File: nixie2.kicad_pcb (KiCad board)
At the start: 2 copper layers, 68.5 x 181 mm, 50 parts, among them J1 AVR-ISP-6, J14 Conn_01x10_Female, SW1 Conn_01x02_Male, SW2 Conn_01x02_Male, SW3 Conn_01x02_Male, SW4 Conn_01x02_Male, SW5 Conn_01x02_Male, SW6 Conn_01x02_Male, U1 ATmega8-16PU, U10 74141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

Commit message: Update.
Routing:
- net GND: track 461.4 -> 464.1 mm
- net Net-(C2-Pad1): track 32.9 -> 35.4 mm
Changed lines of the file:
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@@
     (thickness 1.6)
     (drawings 11)
-    (tracks 781)
+    (tracks 782)
     (zones 0)
     (modules 50)
@@
   )
   (setup
-    (last_trace_width 0.25)
+    (last_trace_width 1)
+    (user_trace_width 1)
     (trace_clearance 0.2)
     (zone_clearance 0.508)
@@
   (segment (start 89.734999 69.975001) (end 97.26 62.45) (width 0.25) (layer B.Cu) (net 4))
   (segment (start 89.545001 69.975001) (end 89.734999 69.975001) (width 0.25) (layer B.Cu) (net 4))
-  (segment (start 108.657499 50.657499) (end 106.15 53.164998) (width 0.25) (layer B.Cu) (net 4))
-  (segment (start 109.419999 49.894999) (end 108.657499 50.657499) (width 0.25) (layer B.Cu) (net 4))
-  (segment (start 86.63 68) (end 87.1 67.53) (width 0.25) (layer F.Cu) (net 4))
-  (segment (start 83 68) (end 86.63 68) (width 0.25) (layer F.Cu) (net 4))
-  (segment (start 88.175001 179.095001) (end 84.56 175.48) (width 0.25) (layer F.Cu) (net 4))
-  (segment (start 88.175001 184.864999) (end 88.175001 179.095001) (width 0.25) (layer F.Cu) (net 4))
-  (segment (start 87 186.04) (end 88.175001 184.864999) (width 0.25) (layer F.Cu) (net 4))
-  (segment (start 87 188.58) (end 87 186.04) (width 0.25) (layer F.Cu) (net 4))
-  (segment (start 87.305001 185.734999) (end 87 186.04) (width 0.25) (layer F.Cu) (net 4))
-  (segment (start 129.507082 185.734999) (end 87.305001 185.734999) (width 0.25) (layer F.Cu) (net 4))
+  (segment (start 109.419999 49.894999) (end 106.15 53.164998) (width 0.25) (layer B.Cu) (net 4))
+  (segment (start 86.63 68) (end 87.1 67.53) (width 0.25) (layer F.Cu) (net 4) (status 30))
+  (segment (start 83 68) (end 86.63 68) (width 0.25) (layer F.Cu) (net 4) (status 30))
+  (segment (start 87 188.58) (end 87 186.04) (width 0.25) (layer F.Cu) (net 4) (status 30))
+  (segment (start 87.305001 185.734999) (end 87 186.04) (width 0.25) (layer F.Cu) (net 4) (status 30))
+  (segment (start 129.507082 185.734999) (end 87.305001 185.734999) (width 0.25) (layer F.Cu) (net 4) (status 20))
   (segment (start 135 180.242081) (end 129.507082 185.734999) (width 0.25) (layer F.Cu) (net 4))
-  (segment (start 135 179.04) (end 135 180.242081) (width 0.25) (layer F.Cu) (net 4))
+  (segment (start 135 179.04) (end 135 180.242081) (width 0.25) (layer F.Cu) (net 4) (status 10))
+  (segment (start 88.202081 186.04) (end 90.5 183.742081) (width 1) (layer F.Cu) (net 4))
+  (segment (start 87 186.04) (end 88.202081 186.04) (width 1) (layer F.Cu) (net 4) (status 10))
+  (segment (start 90.5 181.42) (end 84.56 175.48) (width 1) (layer F.Cu) (net 4) (status 20))
+  (segment (start 90.5 183.742081) (end 90.5 181.42) (width 1) (layer F.Cu) (net 4))
   (segment (start 94.575001 90.245001) (end 93.45 89.12) (width 0.25) (layer B.Cu) (net 6) (status 20))
   (segment (start 107.564999 90.245001) (end 94.575001 90.245001) (width 0.25) (layer B.Cu) (net 6))
@@
   (segment (start 105.01 64.99) (end 110.355002 64.99) (width 0.25) (layer F.Cu) (net 6))
   (segment (start 104.484998 64.99) (end 105.01 64.99) (width 0.25) (layer F.Cu) (net 6))
-  (segment (start 86.53 69.5) (end 87.1 70.07) (width 0.25) (layer F.Cu) (net 6))
-  (segment (start 83 69.5) (end 86.53 69.5) (width 0.25) (layer F.Cu) (net 6))
+  (segment (start 86.53 69.5) (end 87.1 70.07) (width 0.25) (layer F.Cu) (net 6) (status 30))
+  (segment (start 83 69.5) (end 86.53 69.5) (width 0.25) (layer F.Cu) (net 6) (status 30))
   (segment (start 87.005001 79.054999) (end 97.165001 79.054999) (width 0.25) (layer F.Cu) (net 7))
   (segment (start 85.83 80.23) (end 87.005001 79.054999) (width 0.25) (layer F.Cu) (net 7) (status 10))
@@
   (segment (start 84.56 172.94) (end 94.72 172.94) (width 0.25) (layer F.Cu) (net 13) (status 30))
   (segment (start 94.72 172.94) (end 94.72 162.78) (width 0.25) (layer F.Cu) (net 13) (status 30))
-  (segment (start 83.384999 174.115001) (end 84.56 172.94) (width 0.25) (layer F.Cu) (net 13))
-  (segment (start 83.384999 179.884999) (end 83.384999 174.115001) (width 0.25) (layer F.Cu) (net 13))
-  (segment (start 87 183.5) (end 83.384999 179.884999) (width 0.25) (layer F.Cu) (net 13))
+  (segment (start 84.56 172.94) (end 81.5 176) (width 1) (layer F.Cu) (net 13) (status 10))
+  (segment (start 85.266 183.5) (end 87 183.5) (width 1) (layer F.Cu) (net 13) (status 20))
+  (segment (start 81.5 179.734) (end 85.266 183.5) (width 1) (layer F.Cu) (net 13))
+  (segment (start 81.5 176) (end 81.5 179.734) (width 1) (layer F.Cu) (net 13))
   (segment (start 87.1 64.99) (end 90.91 68.8) (width 0.25) (layer F.Cu) (net 14) (status 10))
   (segment (start 90.91 73.88) (end 94.72 77.69) (width 0.25) (layer F.Cu) (net 14) (status 20))
@@
   (segment (start 112.895002 64.115002) (end 109.96 61.18) (width 0.25) (layer B.Cu) (net 115) (status 20))
   (segment (start 113.77 64.115002) (end 112.895002 64.115002) (width 0.25) (layer B.Cu) (net 115))
-  (segment (start 134.5 168) (end 134.5 164) (width 0.25) (layer B.Cu) (net 116))
-  (segment (start 134 140) (end 134.5 140.5) (width 0.25) (layer B.Cu) (net 117))
-  (segment (start 134 135) (end 134 140) (width 0.25) (layer B.Cu) (net 117))
-  (segment (start 135.5 112.5) (end 135.5 105.5) (width 0.25) (layer B.Cu) (net 118))
-  (segment (start 135.5 84.5) (end 135.5 76.5) (width 0.25) (layer B.Cu) (net 119))
-  (segment (start 135 53) (end 135 47) (width 0.25) (layer B.Cu) (net 120))
-  (segment (start 135 30.5) (end 135 23) (width 0.25) (layer B.Cu) (net 121))
-  (segment (start 138.14999 58.68999) (end 135 55.54) (width 0.25) (layer B.Cu) (net 122))
+  (segment (start 134.5 168) (end 134.5 164) (width 0.25) (layer B.Cu) (net 116) (status 30))
+  (segment (start 134 140) (end 134.5 140.5) (width 0.25) (layer B.Cu) (net 117) (status 30))
+  (segment (start 134 135) (end 134 140) (width 0.25) (layer B.Cu) (net 117) (status 30))
+  (segment (start 135.5 112.5) (end 135.5 105.5) (width 0.25) (layer B.Cu) (net 118) (status 30))
+  (segment (start 135.5 84.5) (end 135.5 76.5) (width 0.25) (layer B.Cu) (net 119) (status 30))
+  (segment (start 135 53) (end 135 47) (width 0.25) (layer B.Cu) (net 120) (status 30))
+  (segment (start 135 30.5) (end 135 23) (width 0.25) (layer B.Cu) (net 121) (status 30))
+  (segment (start 138.14999 58.68999) (end 135 55.54) (width 0.25) (layer B.Cu) (net 122) (status 20))
   (segment (start 138.14999 84.39001) (end 138.14999 58.68999) (width 0.25) (layer B.Cu) (net 122))
-  (segment (start 135.5 87.04) (end 138.14999 84.39001) (width 0.25) (layer B.Cu) (net 122))
-  (segment (start 135 55.54) (end 137.5 53.04) (width 0.25) (layer B.Cu) (net 122))
-  (segment (start 137.5 35.54) (end 135 33.04) (width 0.25) (layer B.Cu) (net 122))
+  (segment (start 135.5 87.04) (end 138.14999 84.39001) (width 0.25) (layer B.Cu) (net 122) (status 10))
+  (segment (start 135 55.54) (end 137.5 53.04) (width 0.25) (layer B.Cu) (net 122) (status 10))
+  (segment (start 137.5 35.54) (end 135 33.04) (width 0.25) (layer B.Cu) (net 122) (status 20))
   (segment (start 137.5 53.04) (end 137.5 35.54) (width 0.25) (layer B.Cu) (net 122))
-  (segment (start 138.14999 112.39001) (end 135.5 115.04) (width 0.25) (layer B.Cu) (net 122))
+  (segment (start 138.14999 112.39001) (end 135.5 115.04) (width 0.25) (layer B.Cu) (net 122) (status 20))
   (segment (start 138.14999 89.68999) (end 138.14999 112.39001) (width 0.25) (layer B.Cu) (net 122))
-  (segment (start 135.5 87.04) (end 138.14999 89.68999) (width 0.25) (layer B.Cu) (net 122))
+  (segment (start 135.5 87.04) (end 138.14999 89.68999) (width 0.25) (layer B.Cu) (net 122) (status 10))
   (segment (start 138.14999 117.68999) (end 138.14999 123.85001) (width 0.25) (layer B.Cu) (net 122))
-  (segment (start 135.5 115.04) (end 138.14999 117.68999) (width 0.25) (layer B.Cu) (net 122))
+  (segment (start 135.5 115.04) (end 138.14999 117.68999) (width 0.25) (layer B.Cu) (net 122) (status 10))
   (segment (start 138.14999 123.85001) (end 138 124) (width 0.25) (layer B.Cu) (net 122))
-  (segment (start 138 139.54) (end 134.5 143.04) (width 0.25) (layer B.Cu) (net 122))
+  (segment (start 138 139.54) (end 134.5 143.04) (width 0.25) (layer B.Cu) (net 122) (status 20))
   (segment (start 138 124) (end 138 139.54) (width 0.25) (layer B.Cu) (net 122))
-  (segment (start 138.14999 166.89001) (end 134.5 170.54) (width 0.25) (layer B.Cu) (net 122))
+  (segment (start 138.14999 166.89001) (end 134.5 170.54) (width 0.25) (layer B.Cu) (net 122) (status 20))
   (segment (start 138.14999 146.68999) (end 138.14999 166.89001) (width 0.25) (layer B.Cu) (net 122))
-  (segment (start 134.5 143.04) (end 138.14999 146.68999) (width 0.25) (layer B.Cu) (net 122))
-  (segment (start 134.5 176) (end 135 176.5) (width 0.25) (layer B.Cu) (net 122))
-  (segment (start 134.5 170.54) (end 134.5 176) (width 0.25) (layer B.Cu) (net 122))
+  (segment (start 134.5 143.04) (end 138.14999 146.68999) (width 0.25) (layer B.Cu) (net 122) (status 10))
+  (segment (start 134.5 176) (end 135 176.5) (width 0.25) (layer B.Cu) (net 122) (status 30))
+  (segment (start 134.5 170.54) (end 134.5 176) (width 0.25) (layer B.Cu) (net 122) (status 30))
 )

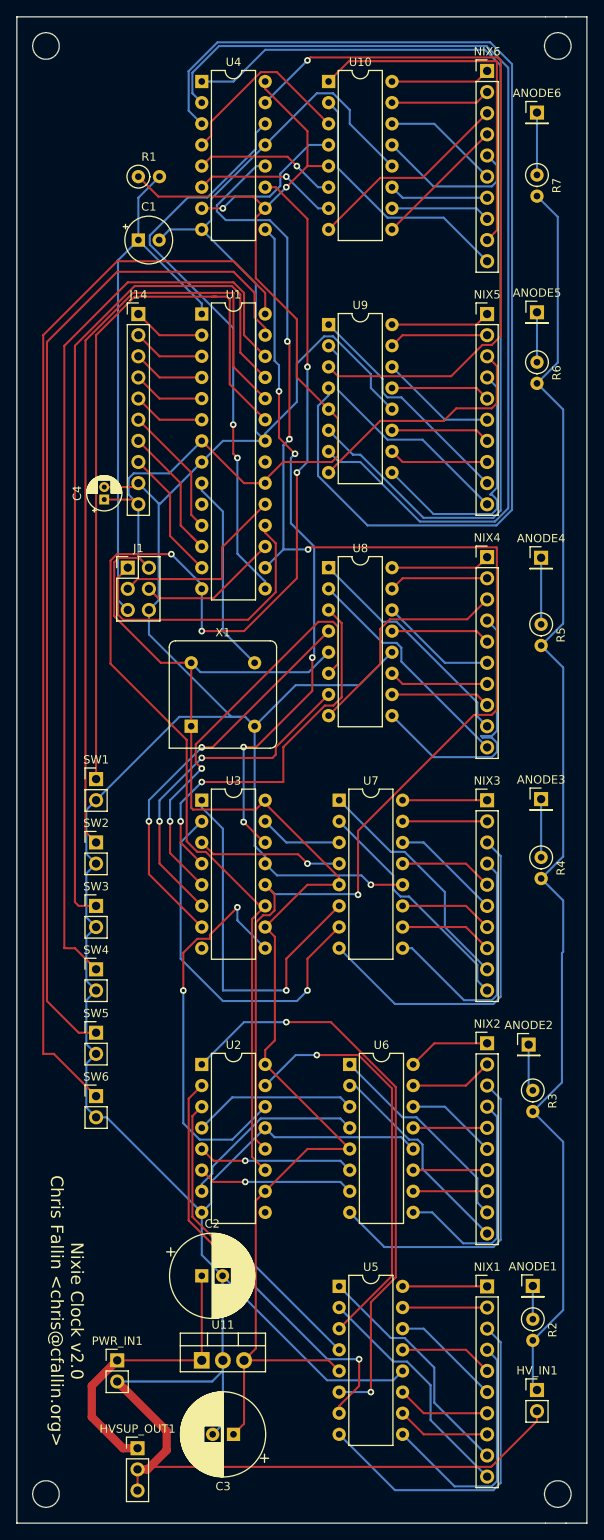
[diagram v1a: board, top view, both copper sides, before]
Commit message: Add tube adapter board, and tweak main board
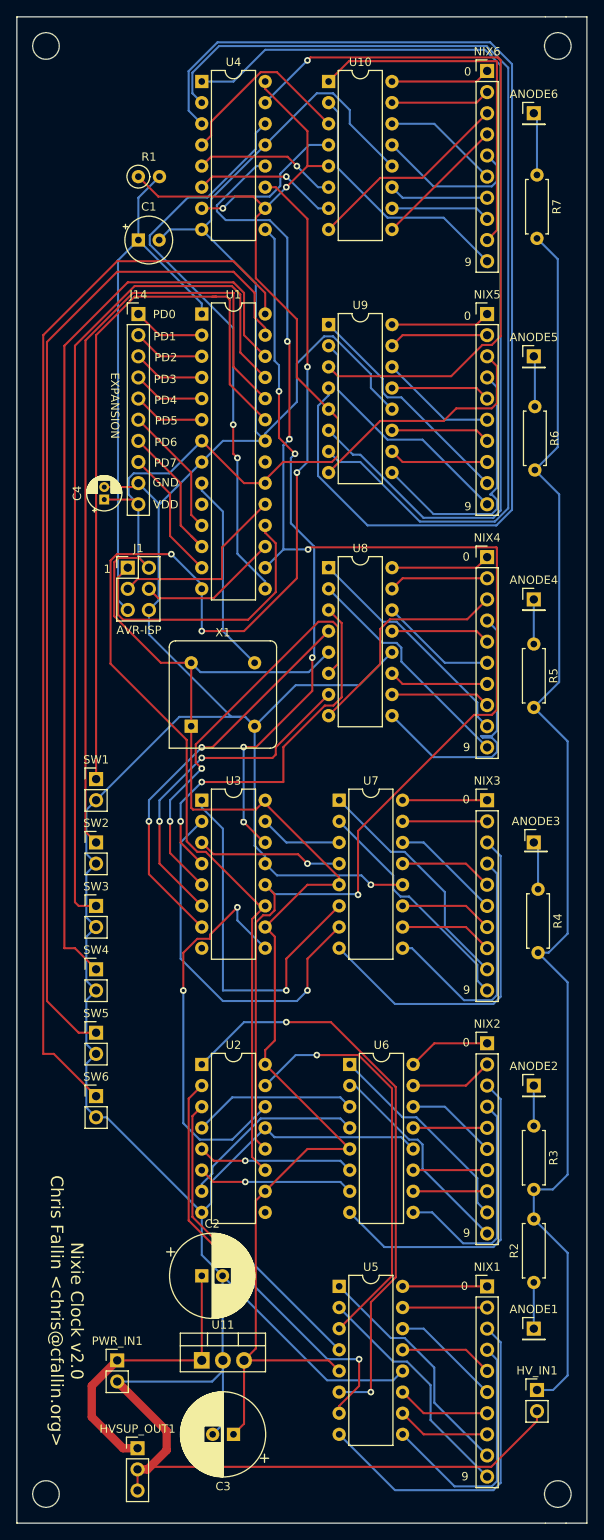
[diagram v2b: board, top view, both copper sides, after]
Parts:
- R2, R3, R4, R5, R6, R7: footprint Resistor_THT:R_Axial_DIN0207_L6.3mm_D2.5mm_P2.54mm_Vertical -> Resistor_THT:R_Axial_DIN0207_L6.3mm_D2.5mm_P7.62mm_Horizontal
- moved ANODE5 5.35 mm to (134.6, 52.3)
- moved R6 5.34 mm to (134.7, 58.3)
- moved ANODE1 5.13 mm to (134.6, 169.1)
- moved ANODE4 5.08 mm to (134.6, 81.5)
- moved ANODE3 5.03 mm to (134.9, 110.5)
- moved ANODE2 4.96 mm to (134.6, 139.9)
- moved R2 4.43 mm to (134.6, 163.6), turned to 90 degrees
- moved R3 4.28 mm to (134.6, 144.8)
- moved R4 3.85 mm to (135.1, 116.3)
- moved R5 2.53 mm to (134.6, 86.9)
- moved ANODE6 0.40 mm to (134.6, 23.1)
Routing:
- net Net-(ANODE4-Pad1): track 8.00 -> 5.37 mm
- net Net-(ANODE1-Pad1): track 4.00 -> 5.55 mm
- net Net-(ANODE3-Pad1): track 7.00 -> 5.83 mm
- net Net-(ANODE2-Pad1): track 5.71 -> 4.86 mm
- net Net-(HV_IN1-Pad1): track 156.0 -> 156.5 mm
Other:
- board text added: "0"
- board text added: "1"
- board text added: "9"
- board text added: "AVR-ISP"
- board text added: "EXPANSION"
- board text added: "GND"
- board text added: "PD0"
- board text added: "PD1"
- board text added: "PD2"
- board text added: "PD3"
- board text added: "PD4"
- board text added: "PD5"
- board text added: "PD6"
- board text added: "PD7"
- board text added: "VDD"

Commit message: Add some mounting holes
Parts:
- added REF**: MountingHole_3.2mm_M3, MountingHole:MountingHole_3.2mm_M3, F.Cu at (108.5, 101.0)
